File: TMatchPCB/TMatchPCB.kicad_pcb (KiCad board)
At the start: 2 copper layers, 100 x 100 mm, 28 parts, among them J1 CapPlate, J2 CapPlate, J3 BNC, J4 CapPlate, J5 CapPlate, J6 BNC, SW1 SW_SPST, SW2 SW_SPST, SW3 SW_SPST, SW4 SW_SPST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

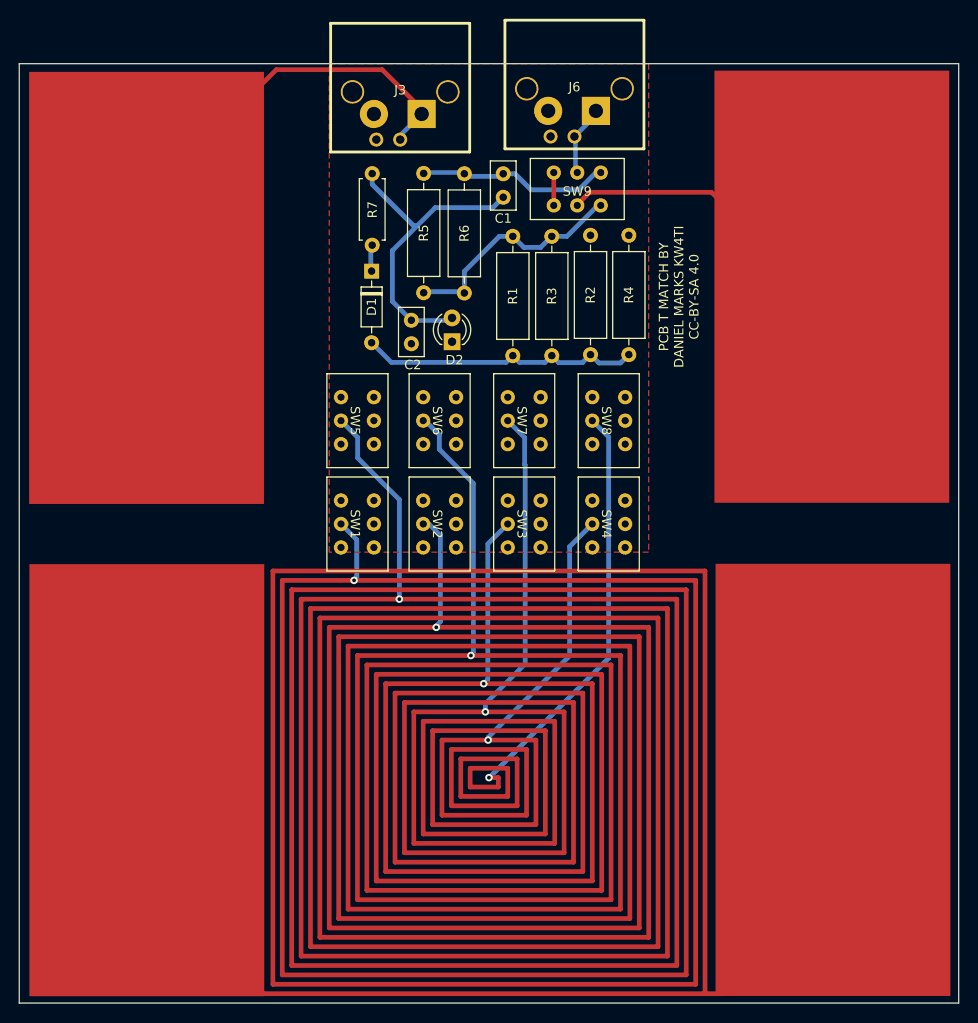
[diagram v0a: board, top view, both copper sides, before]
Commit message: Added vernier lines
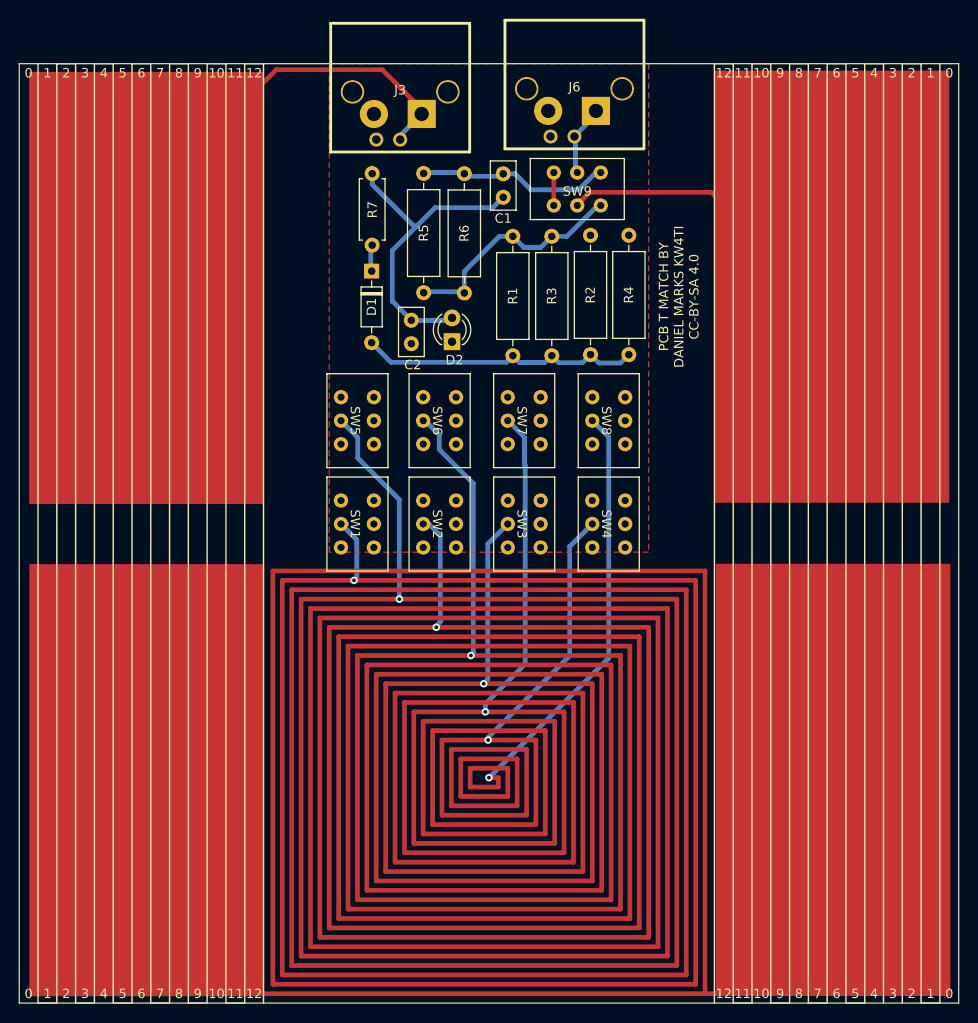
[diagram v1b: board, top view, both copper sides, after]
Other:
- board text added: "0"
- board text added: "1"
- board text added: "10"
- board text added: "11"
- board text added: "12"
- board text added: "2"
- board text added: "3"
- board text added: "4"
- board text added: "5"
- board text added: "6"
- board text added: "7"
- board text added: "8"
- board text added: "9"
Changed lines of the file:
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@@
       (net 6 "Net-(SW9-Pad6)") (pinfunction "C") (pintype "passive"))
   )
+  (gr_line (start 30 120) (end 32 120) (layer "F.SilkS") (width 0.15))
+  (gr_line (start 112 120) (end 112 20) (layer "F.SilkS") (width 0.15))
+  (gr_line (start 116 120) (end 116 20) (layer "F.SilkS") (width 0.15))
+  (gr_line (start 100 120) (end 100 20) (layer "F.SilkS") (width 0.15))
+  (gr_line (start 106 20) (end 106 120) (layer "F.SilkS") (width 0.15))
+  (gr_line (start 34 120) (end 36 120) (layer "F.SilkS") (width 0.15))
+  (gr_line (start 98 20) (end 98 120) (layer "F.SilkS") (width 0.15))
+  (gr_line (start 36 20) (end 38 20) (layer "F.SilkS") (width 0.15))
+  (gr_line (start 114 20) (end 114 120) (layer "F.SilkS") (width 0.15))
+  (gr_line (start 96 120) (end 96 20) (layer "F.SilkS") (width 0.15))
+  (gr_line (start 40 20) (end 42 20) (layer "F.SilkS") (width 0.15))
+  (gr_line (start 108 20) (end 106 20) (layer "F.SilkS") (width 0.15))
+  (gr_line (start 44 20) (end 46 20) (layer "F.SilkS") (width 0.15))
+  (gr_line (start 98 120) (end 96 120) (layer "F.SilkS") (width 0.15))
+  (gr_line (start 110 120) (end 108 120) (layer "F.SilkS") (width 0.15))
+  (gr_line (start 46 20) (end 46 120) (layer "F.SilkS") (width 0.15))
+  (gr_line (start 102 120) (end 100 120) (layer "F.SilkS") (width 0.15))
+  (gr_line (start 24 120) (end 24 20) (layer "F.SilkS") (width 0.15))
+  (gr_line (start 100 20) (end 98 20) (layer "F.SilkS") (width 0.15))
+  (gr_line (start 116 20) (end 114 20) (layer "F.SilkS") (width 0.15))
+  (gr_line (start 24 20) (end 26 20) (layer "F.SilkS") (width 0.15))
+  (gr_line (start 108 120) (end 108 20) (layer "F.SilkS") (width 0.15))
+  (gr_line (start 112 20) (end 110 20) (layer "F.SilkS") (width 0.15))
+  (gr_line (start 32 20) (end 34 20) (layer "F.SilkS") (width 0.15))
+  (gr_line (start 118 120) (end 116 120) (layer "F.SilkS") (width 0.15))
+  (gr_line (start 42 20) (end 42 120) (layer "F.SilkS") (width 0.15))
+  (gr_line (start 44 120) (end 44 20) (layer "F.SilkS") (width 0.15))
+  (gr_line (start 22 120) (end 24 120) (layer "F.SilkS") (width 0.15))
+  (gr_line (start 28 120) (end 28 20) (layer "F.SilkS") (width 0.15))
+  (gr_line (start 28 20) (end 30 20) (layer "F.SilkS") (width 0.15))
+  (gr_line (start 102 20) (end 102 120) (layer "F.SilkS") (width 0.15))
+  (gr_line (start 118 20) (end 118 120) (layer "F.SilkS") (width 0.15))
+  (gr_line (start 32 120) (end 32 20) (layer "F.SilkS") (width 0.15))
+  (gr_line (start 40 120) (end 40 20) (layer "F.SilkS") (width 0.15))
+  (gr_line (start 38 120) (end 40 120) (layer "F.SilkS") (width 0.15))
+  (gr_line (start 26 120) (end 28 120) (layer "F.SilkS") (width 0.15))
+  (gr_line (start 42 120) (end 44 120) (layer "F.SilkS") (width 0.15))
+  (gr_line (start 34 20) (end 34 120) (layer "F.SilkS") (width 0.15))
+  (gr_line (start 36 120) (end 36 20) (layer "F.SilkS") (width 0.15))
+  (gr_line (start 110 20) (end 110 120) (layer "F.SilkS") (width 0.15))
+  (gr_line (start 38 20) (end 38 120) (layer "F.SilkS") (width 0.15))
+  (gr_line (start 104 120) (end 104 20) (layer "F.SilkS") (width 0.15))
+  (gr_line (start 104 20) (end 102 20) (layer "F.SilkS") (width 0.15))
+  (gr_line (start 94 20) (end 94 120) (layer "F.SilkS") (width 0.15))
+  (gr_line (start 96 20) (end 94 20) (layer "F.SilkS") (width 0.15))
+  (gr_line (start 106 120) (end 104 120) (layer "F.SilkS") (width 0.15))
+  (gr_line (start 26 20) (end 26 120) (layer "F.SilkS") (width 0.15))
+  (gr_line (start 22 20) (end 22 120) (layer "F.SilkS") (width 0.15))
+  (gr_line (start 30 20) (end 30 120) (layer "F.SilkS") (width 0.15))
   (gr_line (start 20 20) (end 120 20) (layer "Edge.Cuts") (width 0.1))
   (gr_line (start 120 20) (end 120 120) (layer "Edge.Cuts") (width 0.1))
   (gr_line (start 120 120) (end 20 120) (layer "Edge.Cuts") (width 0.1))
   (gr_line (start 20 120) (end 20 20) (layer "Edge.Cuts") (width 0.1))
+  (gr_text "6" (at 107 21) (layer "F.SilkS")
+    (effects (font (size 1 1) (thickness 0.15)))
+  )
+  (gr_text "0" (at 119 21) (layer "F.SilkS")
+    (effects (font (size 1 1) (thickness 0.15)))
+  )
+  (gr_text "9" (at 39 21) (layer "F.SilkS")
+    (effects (font (size 1 1) (thickness 0.15)))
+  )
+  (gr_text "9" (at 101 119) (layer "F.SilkS")
+    (effects (font (size 1 1) (thickness 0.15)))
+  )
+  (gr_text "0" (at 21 21) (layer "F.SilkS")
+    (effects (font (size 1 1) (thickness 0.15)))
+  )
+  (gr_text "3" (at 113 21) (layer "F.SilkS")
+    (effects (font (size 1 1) (thickness 0.15)))
+  )
+  (gr_text "0" (at 119 119) (layer "F.SilkS")
+    (effects (font (size 1 1) (thickness 0.15)))
+  )
+  (gr_text "2" (at 115 119) (layer "F.SilkS")
+    (effects (font (size 1 1) (thickness 0.15)))
+  )
+  (gr_text "5" (at 31 119) (layer "F.SilkS")
+    (effects (font (size 1 1) (thickness 0.15)))
+  )
+  (gr_text "2" (at 25 21) (layer "F.SilkS")
+    (effects (font (size 1 1) (thickness 0.15)))
+  )
   (gr_text "PCB T MATCH BY\nDANIEL MARKS KW4TI\nCC-BY-SA 4.0\n" (at 90.23 44.81 90) (layer "F.SilkS")
     (effects (font (size 1 1) (thickness 0.15)))
   )
+  (gr_text "12" (at 45 21) (layer "F.SilkS")
+    (effects (font (size 1 1) (thickness 0.15)))
+  )
+  (gr_text "10" (at 41 21) (layer "F.SilkS")
+    (effects (font (size 1 1) (thickness 0.15)))
+  )
+  (gr_text "10" (at 99 119) (layer "F.SilkS")
+    (effects (font (size 1 1) (thickness 0.15)))
+  )
+  (gr_text "3" (at 113 119) (layer "F.SilkS")
+    (effects (font (size 1 1) (thickness 0.15)))
+  )
+  (gr_text "6" (at 107 119) (layer "F.SilkS")
+    (effects (font (size 1 1) (thickness 0.15)))
+  )
+  (gr_text "1" (at 117 119) (layer "F.SilkS")
+    (effects (font (size 1 1) (thickness 0.15)))
+  )
+  (gr_text "12" (at 95 119) (layer "F.SilkS")
+    (effects (font (size 1 1) (thickness 0.15)))
+  )
+  (gr_text "4" (at 29 21) (layer "F.SilkS")
+    (effects (font (size 1 1) (thickness 0.15)))
+  )
+  (gr_text "8" (at 37 119) (layer "F.SilkS")
+    (effects (font (size 1 1) (thickness 0.15)))
+  )
+  (gr_text "11" (at 97 21) (layer "F.SilkS")
+    (effects (font (size 1 1) (thickness 0.15)))
+  )
+  (gr_text "11" (at 97 119) (layer "F.SilkS")
+    (effects (font (size 1 1) (thickness 0.15)))
+  )
+  (gr_text "9" (at 39 119) (layer "F.SilkS")
+    (effects (font (size 1 1) (thickness 0.15)))
+  )
+  (gr_text "5" (at 31 21) (layer "F.SilkS")
+    (effects (font (size 1 1) (thickness 0.15)))
+  )
+  (gr_text "10" (at 99 21) (layer "F.SilkS")
+    (effects (font (size 1 1) (thickness 0.15)))
+  )
+  (gr_text "7" (at 105 119) (layer "F.SilkS")
+    (effects (font (size 1 1) (thickness 0.15)))
+  )
+  (gr_text "11" (at 43 119) (layer "F.SilkS")
+    (effects (font (size 1 1) (thickness 0.15)))
+  )
+  (gr_text "3" (at 27 119) (layer "F.SilkS")
+    (effects (font (size 1 1) (thickness 0.15)))
+  )
+  (gr_text "4" (at 111 21) (layer "F.SilkS")
+    (effects (font (size 1 1) (thickness 0.15)))
+  )
+  (gr_text "1" (at 23 119) (layer "F.SilkS")
+    (effects (font (size 1 1) (thickness 0.15)))
+  )
+  (gr_text "5" (at 109 119) (layer "F.SilkS")
+    (effects (font (size 1 1) (thickness 0.15)))
+  )
+  (gr_text "12" (at 95 21) (layer "F.SilkS")
+    (effects (font (size 1 1) (thickness 0.15)))
+  )
+  (gr_text "6" (at 33 119) (layer "F.SilkS")
+    (effects (font (size 1 1) (thickness 0.15)))
+  )
+  (gr_text "1" (at 23 21) (layer "F.SilkS")
+    (effects (font (size 1 1) (thickness 0.15)))
+  )
+  (gr_text "11" (at 43 21) (layer "F.SilkS")
+    (effects (font (size 1 1) (thickness 0.15)))
+  )
+  (gr_text "4" (at 29 119) (layer "F.SilkS")
+    (effects (font (size 1 1) (thickness 0.15)))
+  )
+  (gr_text "9" (at 101 21) (layer "F.SilkS")
+    (effects (font (size 1 1) (thickness 0.15)))
+  )
+  (gr_text "2" (at 115 21) (layer "F.SilkS")
+    (effects (font (size 1 1) (thickness 0.15)))
+  )
+  (gr_text "8" (at 103 21) (layer "F.SilkS")
+    (effects (font (size 1 1) (thickness 0.15)))
+  )
+  (gr_text "5" (at 109 21) (layer "F.SilkS")
+    (effects (font (size 1 1) (thickness 0.15)))
+  )
+  (gr_text "7" (at 35 21) (layer "F.SilkS")
+    (effects (font (size 1 1) (thickness 0.15)))
+  )
+  (gr_text "1" (at 117 21) (layer "F.SilkS")
+    (effects (font (size 1 1) (thickness 0.15)))
+  )
+  (gr_text "4" (at 111 119) (layer "F.SilkS")
+    (effects (font (size 1 1) (thickness 0.15)))
+  )
+  (gr_text "3" (at 27 21) (layer "F.SilkS")
+    (effects (font (size 1 1) (thickness 0.15)))
+  )
+  (gr_text "8" (at 37 21) (layer "F.SilkS")
+    (effects (font (size 1 1) (thickness 0.15)))
+  )
+  (gr_text "2" (at 25 119) (layer "F.SilkS")
+    (effects (font (size 1 1) (thickness 0.15)))
+  )
+  (gr_text "0" (at 21 119) (layer "F.SilkS")
+    (effects (font (size 1 1) (thickness 0.15)))
+  )
+  (gr_text "12" (at 45 119) (layer "F.SilkS")
+    (effects (font (size 1 1) (thickness 0.15)))
+  )
+  (gr_text "6" (at 33 21) (layer "F.SilkS")
+    (effects (font (size 1 1) (thickness 0.15)))
+  )
+  (gr_text "8" (at 103 119) (layer "F.SilkS")
+    (effects (font (size 1 1) (thickness 0.15)))
+  )
+  (gr_text "10" (at 41 119) (layer "F.SilkS")
+    (effects (font (size 1 1) (thickness 0.15)))
+  )
+  (gr_text "7" (at 35 119) (layer "F.SilkS")
+    (effects (font (size 1 1) (thickness 0.15)))
+  )
+  (gr_text "7" (at 105 21) (layer "F.SilkS")
+    (effects (font (size 1 1) (thickness 0.15)))
+  )

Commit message: Added more ruled lines
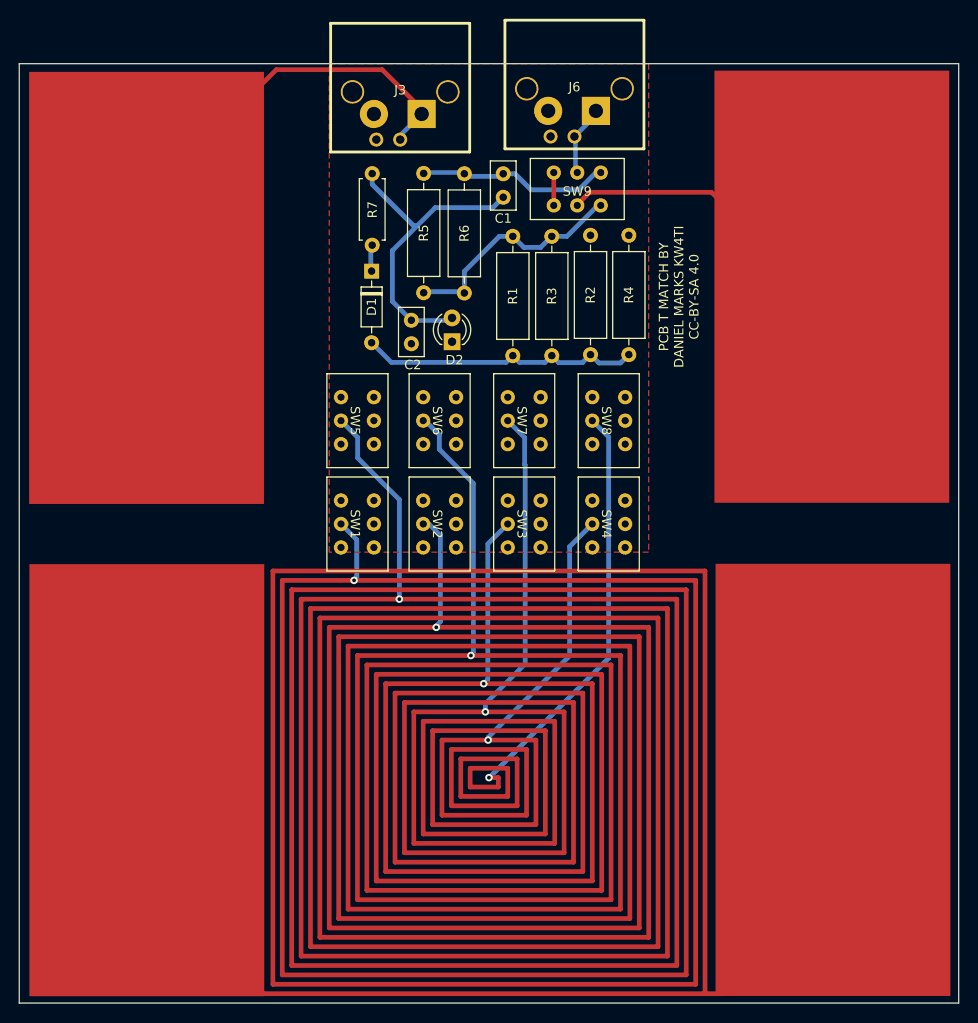
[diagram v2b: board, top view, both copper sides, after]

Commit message: Modified resistive bridge
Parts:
- removed C1, C2: 10 nF, Capacitor_THT:C_Disc_D5.0mm_W2.5mm_P2.50mm
- moved R7 19.0 mm to (57.2, 50.7), turned to 90 degrees
- moved D1 10.2 mm to (57.2, 31.9)
- moved SW9 4.10 mm to (83.5, 35.1)
- moved J3 3.06 mm to (57.5, 15.5)
- moved J6 2.90 mm to (82.0, 15.4)
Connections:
- D1 pad 2: Net-(D1-Pad2) -> Net-(R1-Pad2)
- D2 pad 1: GND -> Net-(D2-Pad1)
- D2 pad 2: Net-(C1-Pad2) -> Net-(D2-Pad2)
- R1 pad 1: Net-(SW9-Pad3) -> Net-(R1-Pad1)
- R1 pad 2: Net-(D1-Pad2) -> Net-(R1-Pad2)
- R2 pad 1: Net-(D1-Pad2) -> Net-(R1-Pad2)
- R3 pad 1: Net-(SW9-Pad3) -> Net-(R1-Pad1)
- R3 pad 2: Net-(D1-Pad2) -> Net-(R1-Pad2)
- R4 pad 1: Net-(D1-Pad2) -> Net-(R1-Pad2)
- R5 pad 1: Net-(SW9-Pad6) -> Net-(D2-Pad2)
- R5 pad 2: Net-(SW9-Pad3) -> Net-(R1-Pad1)
- R6 pad 1: Net-(SW9-Pad6) -> Net-(D2-Pad2)
- R6 pad 2: Net-(SW9-Pad3) -> Net-(R1-Pad1)
- R7 pad 1: Net-(C1-Pad2) -> Net-(R1-Pad2)
- R7 pad 2: Net-(D1-Pad1) -> Net-(D2-Pad1)
- SW9 pad 1: Net-(SW9-Pad1) -> Net-(D2-Pad2)
- SW9 pad 4: Net-(SW9-Pad1) -> Net-(R1-Pad1)
- SW9 pad 6: Net-(SW9-Pad6) -> Net-(SW9-Pad3)
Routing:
- net Net-(D2-Pad2): track 0.00 -> 47.2 mm
- net Net-(R1-Pad2): track 0.00 -> 41.4 mm
- net Net-(C1-Pad2): track 34.6 -> 0.00 mm
- net Net-(D1-Pad2): track 30.5 -> 0.00 mm
- net Net-(R1-Pad1): track 0.00 -> 26.2 mm
- net Net-(J5-Pad1): track 31.9 -> 57.5 mm
- net Net-(SW9-Pad3): track 25.1 -> 3.50 mm
- net Net-(SW9-Pad6): track 20.6 -> 0.00 mm
- net Net-(J3-Pad1): track 57.4 -> 40.9 mm
- net Net-(D2-Pad1): track 0.00 -> 12.5 mm
- net Net-(SW9-Pad1): track 3.50 -> 0.00 mm
- net Net-(D1-Pad1): track 2.85 -> 0.00 mm
- net Net-(J6-Pad1): track 7.64 -> 10.3 mm
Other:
- board text added: "ANTENNA"
- board text added: "BYP"
- board text added: "IND1"
- board text added: "IND2"
- board text added: "IND3"
- board text added: "IND4"
- board text added: "IND5"
- board text added: "IND6"
- board text added: "IND7"
- board text added: "IND8"
- board text added: "MEAS"
- board text added: "TRANSCEIVER"
